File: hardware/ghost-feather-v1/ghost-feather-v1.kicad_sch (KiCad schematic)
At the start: 58 parts, among them J1 Conn_ARM_SWD_TagConnect_TC2030, J2 USB_C_Receptacle_USB2.0, J3 Conn_01x03, J4 Conn_01x03, J5 Conn_01x03, J6 Conn_01x03, J7 Conn_01x08, Q1 BSS138, Q2 BSS138, Q3 BSS138, Q4 BSS138, SW2 BOOT0, U1 STM32F722RETx, U2 BMI270, U3 USBLC6-2SC6_MOD, U6 MPM3610, U7 MPM3610, X1 16MHz, X2 32kHz768

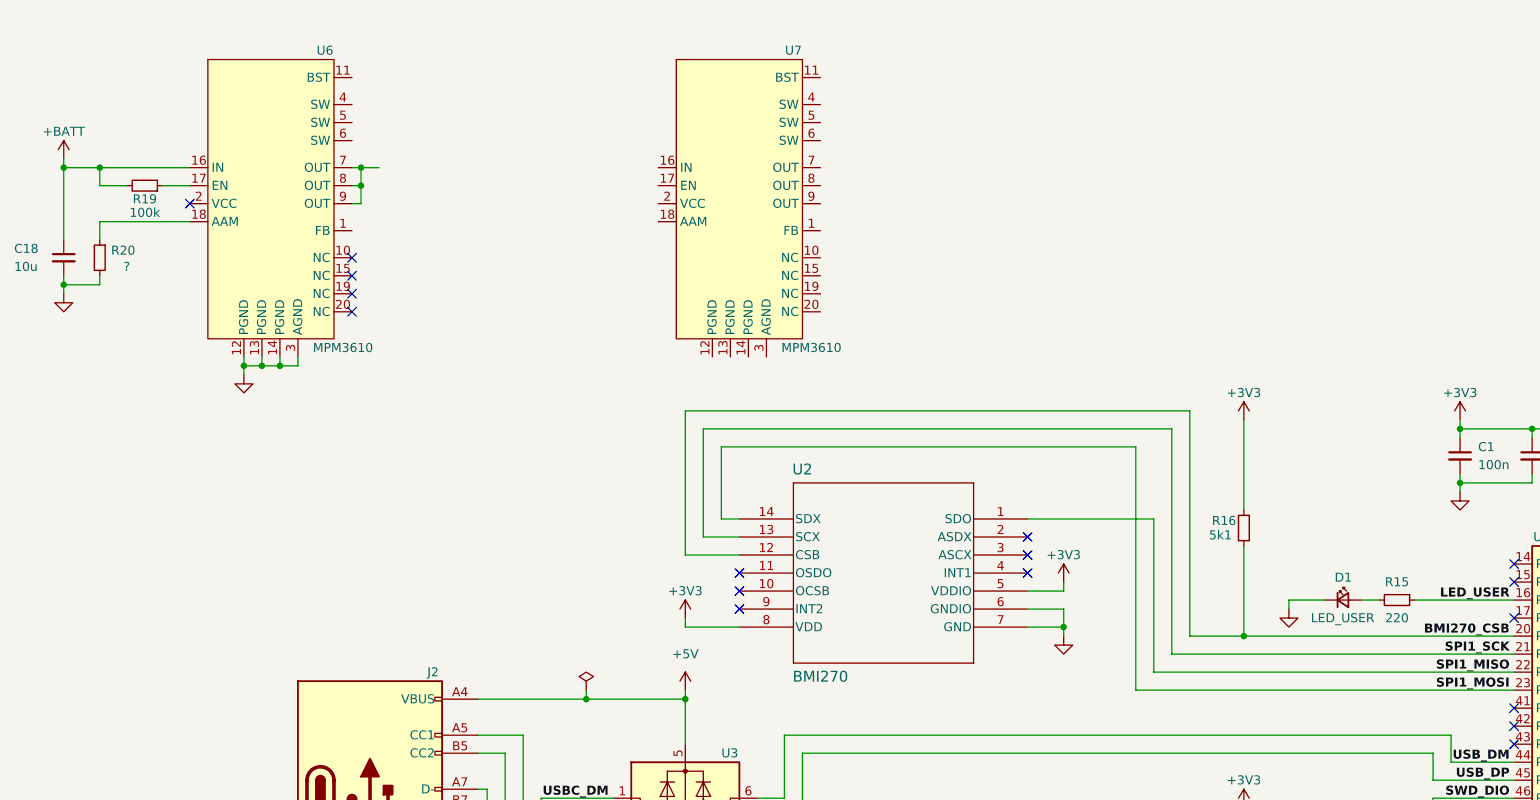
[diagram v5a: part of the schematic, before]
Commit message: feat: Add the MPM3610 switching regulators #2
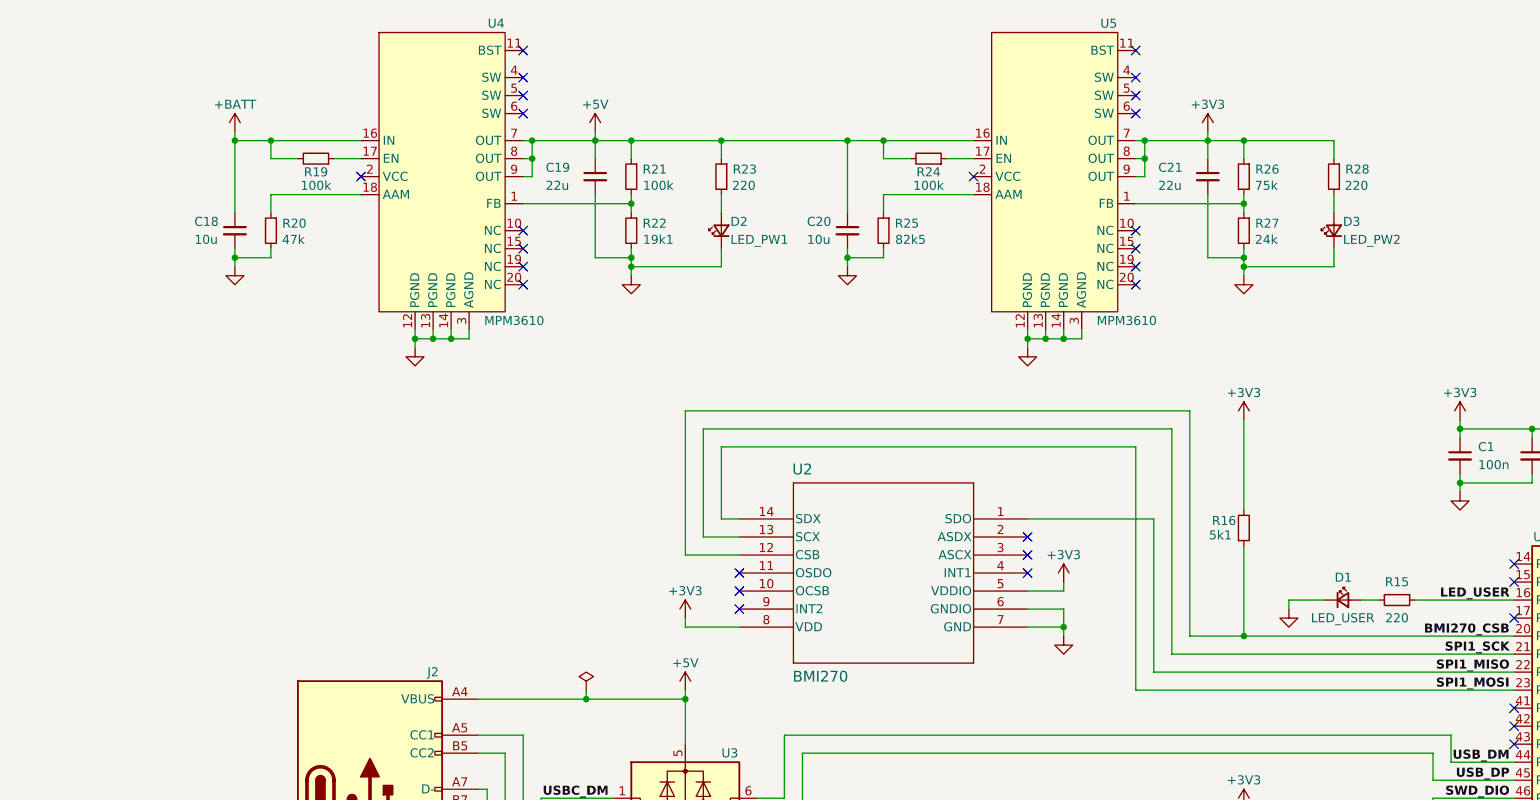
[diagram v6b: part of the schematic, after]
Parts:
- removed U7: MPM3610, symbol ghost-feather-v1:MPM3610
- added C19, C21: 22u, Capacitor_SMD:C_0603_1608Metric, symbol Device:C_Small
- added C20: 10u, Capacitor_SMD:C_0603_1608Metric, symbol Device:C_Small
- added D2: LED_PW1, LED_SMD:LED_0402_1005Metric, symbol Device:LED_Small
- added D3: LED_PW2, LED_SMD:LED_0402_1005Metric, symbol Device:LED_Small
- added R21, R24: 100k, Resistor_SMD:R_0402_1005Metric, symbol Device:R_Small
- added R22: 19k1, Resistor_SMD:R_0402_1005Metric, symbol Device:R_Small
- added R23, R28: 220, Resistor_SMD:R_0402_1005Metric, symbol Device:R_Small
- added R25: 82k5, Resistor_SMD:R_0402_1005Metric, symbol Device:R_Small
- added R26: 75k, Resistor_SMD:R_0402_1005Metric, symbol Device:R_Small
- added R27: 24k, Resistor_SMD:R_0402_1005Metric, symbol Device:R_Small
- added U5: MPM3610, symbol ghost-feather-v1:MPM3610
- R20: value ? -> 47k
- renumbered U6 to U4
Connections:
- net +3V3: now also C21.1, R26.1, R28.1, U5.7 (OUT), U5.8 (OUT), U5.9 (OUT)
- net +5V: now also U4.7 (OUT), U4.8 (OUT), U4.9 (OUT), C19.1, C20.1, R21.1, R23.1, R24.2, U5.16 (IN)
- net GND: now also C19.2, C20.2, C21.2, D2.1 (K), D3.1 (K), R22.2, R25.2, R27.2, U5.12 (PGND), U5.13 (PGND), U5.14 (PGND), U5.3 (AGND)
- net at U4.1 (FB): now also R21.2, R22.1
- new net: D3.2 (A), R28.2
- new net: R24.1, U5.17 (EN)
- new net: D2.2 (A), R23.2
- new net: R26.2, R27.1, U5.1 (FB)
- new net: R25.1, U5.18 (AAM)
- no-connect marks 40 -> 53
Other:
- moved on the sheet: C18, R19, R20, U4

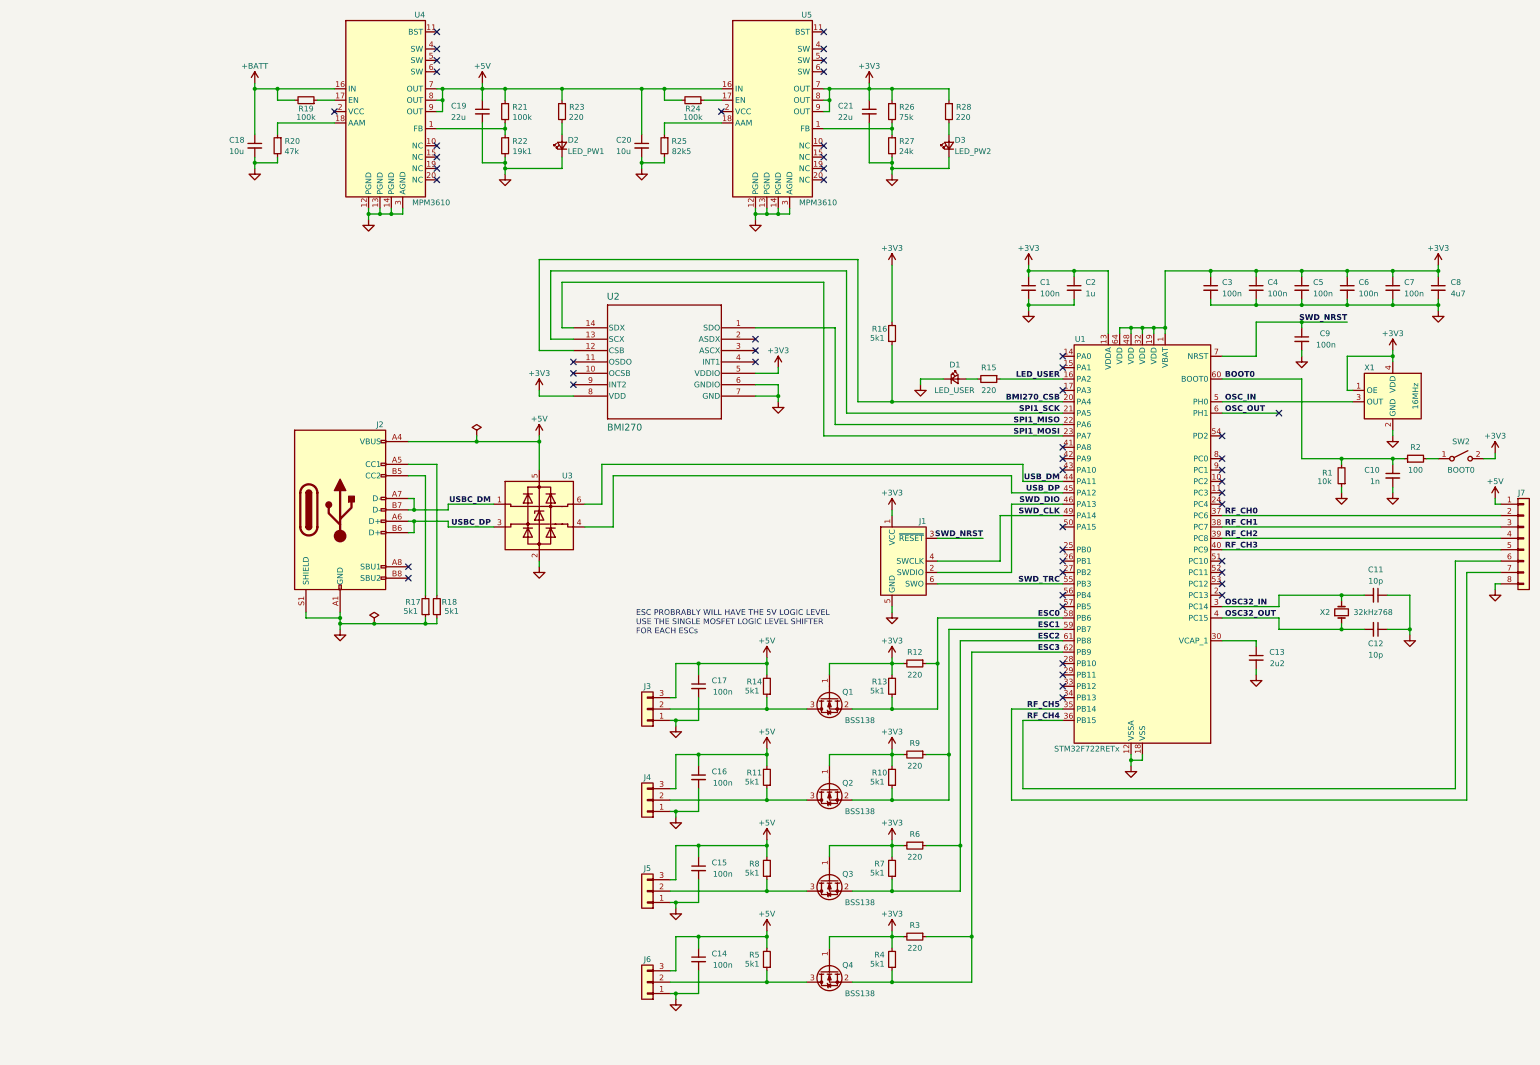
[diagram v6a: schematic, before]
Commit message: doc: Add the page settings
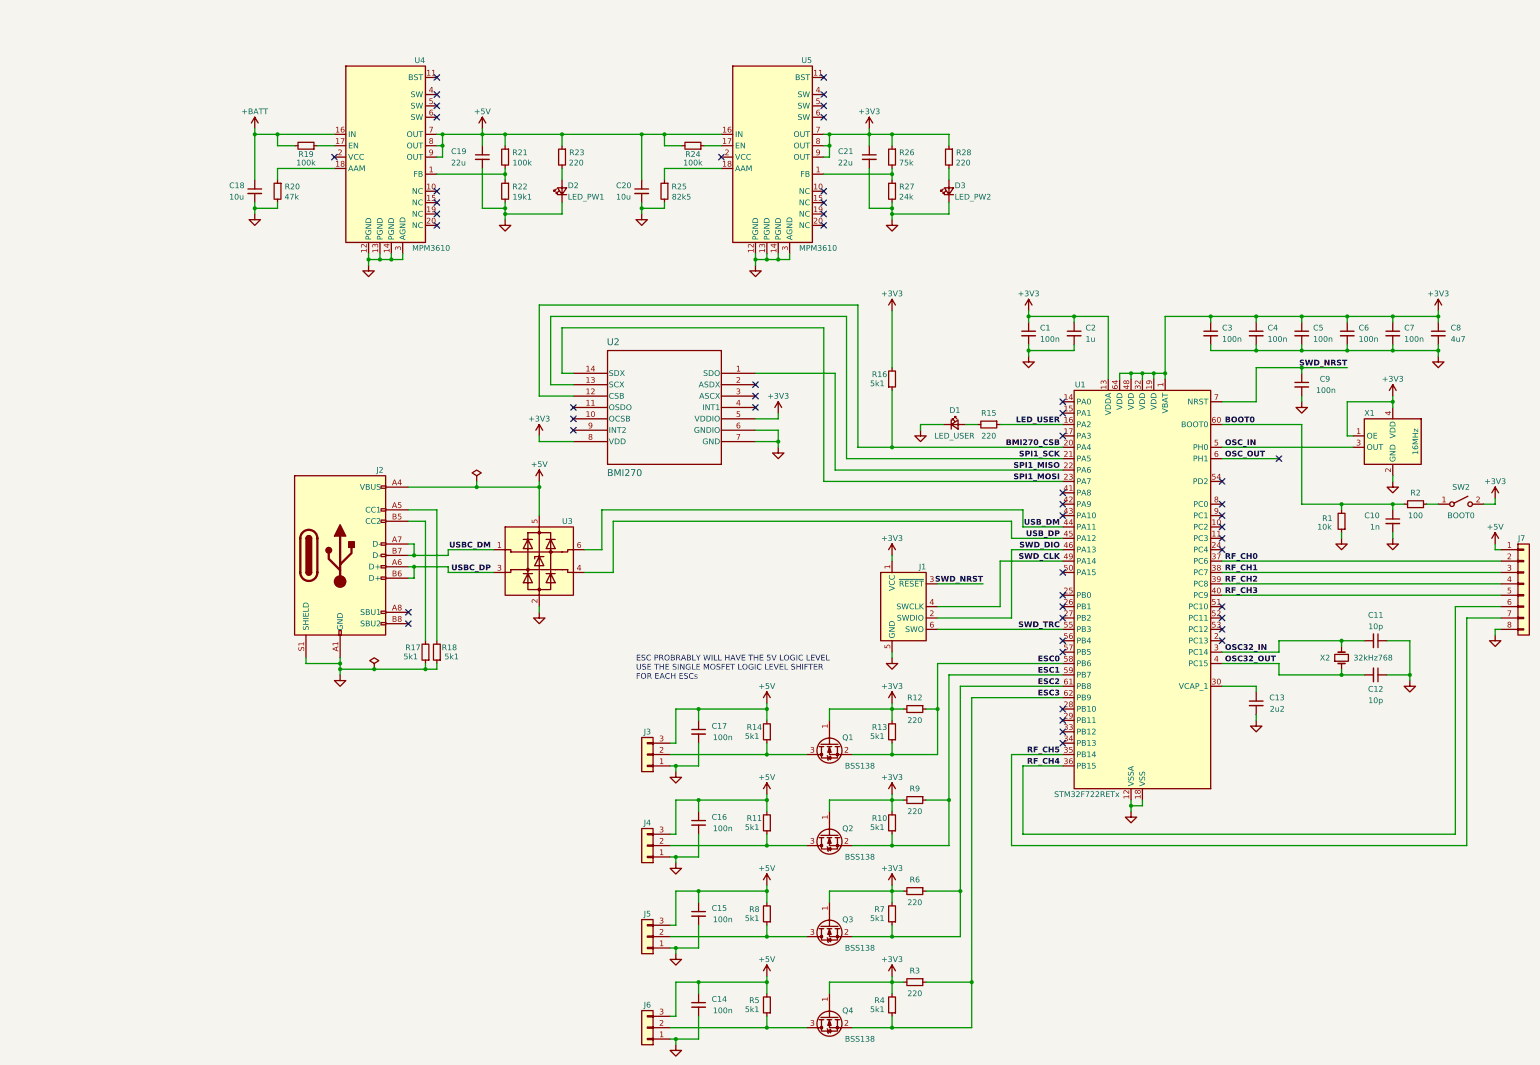
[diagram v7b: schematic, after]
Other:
- title: (none) -> ghost-feather-v1
- moved on the sheet: C1, C10, C11, C12, C13, C14, C15, C16, C17, C18, C19, C2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

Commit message: feat: Assign basic version of MPM3610 footprint
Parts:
- U4, U5: footprint (none) -> ghost-feather-v1:MPM3610
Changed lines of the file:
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@@
       (effects (font (size 1.27 1.27)))
     )
-    (property "Footprint" "" (at 104.14 45.72 0)
+    (property "Footprint" "ghost-feather-v1:MPM3610" (at 104.14 45.72 0)
       (effects (font (size 1.27 1.27)) hide)
     )
@@
       (effects (font (size 1.27 1.27)))
     )
-    (property "Footprint" "" (at 190.5 45.72 0)
-      (effects (font (size 1.27 1.27)) hide)
-    )
+    (property "Footprint" "ghost-feather-v1:MPM3610" (at 190.5 45.72 0)
+      (effects (font (size 1.27 1.27)) hide)
+    )
